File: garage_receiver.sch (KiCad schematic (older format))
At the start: 11 parts, among them J1 Conn_01x04_Female, J2 Screw_Terminal_01x04, Q1 2N7002, SW1 SW_DIP_x08, U1 HT12D

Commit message: DC/DC Converter
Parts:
- removed R1: 47k, Resistor_SMD:R_0805_2012Metric, symbol Device:R
- added C2: 47u, Capacitor_THT:CP_Radial_D5.0mm_P2.00mm, symbol Device:C
- added C3: 2.2u, Capacitor_THT:C_Disc_D4.3mm_W1.9mm_P5.00mm, symbol Device:C
- added D5: 1N5819, Diode_THT:D_DO-41_SOD81_P10.16mm_Horizontal, symbol Diode:1N5819
- added L1: 220u, Inductor_SMD:L_10.4x10.4_H4.8, symbol Device:L
- added Q2: 2N7002, Package_TO_SOT_SMD:SOT-23, symbol Transistor_FET:2N7002
- added R2: 1k, Resistor_SMD:R_0805_2012Metric, symbol Device:R
- added R3: 47k, Resistor_SMD:R_0805_2012Metric, symbol Device:R
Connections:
- net +12V: now also Q2.3 (D), R2.1; no longer D1.1 (K), D3.2 (A), J1.1 (Pin_1), U1.19 (VDD)
- net GND: now also D2.2 (A), D4.1 (K), C2.2, C3.2, D5.2 (A); no longer D3.1 (K), D4.2 (A), J2.2 (Pin_2), J2.3 (Pin_3), Q1.2 (S)
- net rf_data: now reaches J1.2 (Pin_2), J1.3 (Pin_3), U1.15 (DIN)
- net at U1.16 (OSC2): now also R3.2
- net at U1.17 (OSC1): now also R3.1
- net open: now reaches Q1.1 (G), U1.18 (VT)
- net door_control1: now reaches Q1.3 (D)
- net door_control1: now also J2.2 (Pin_2); no longer J2.1 (Pin_1)
- new net: D1.1 (K), D3.2 (A), R2.2
- new net: D5.1 (K), L1.1, Q2.2 (S)
- new net +5V: C2.1, C3.1, J1.1 (Pin_1), L1.2, U1.19 (VDD)
- new net GNDPWR: D3.1 (K), D4.2 (A), J2.3 (Pin_3)
- new net door_control2: J2.1 (Pin_1), Q1.2 (S)
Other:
- note added: "Actuator"
- note added: "DC/DC Converter"
- note added: "Decoder"
- note added: "RF 433/315MHz Receiver"
- note added: "Rectifier"
- note added: "Supply and Control Sinals"
- moved on the sheet: C1, D1, D2, D3, D4, J1, J2, Q1, SW1, U1

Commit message: DC/DC Converter Controller
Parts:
- removed D5: 1N5819, Diode_THT:D_DO-41_SOD81_P10.16mm_Horizontal, symbol Diode:1N5819
- removed Q2: 2N7002, Package_TO_SOT_SMD:SOT-23, symbol Transistor_FET:2N7002
- added C?: 1u, Capacitor_THT:CP_Radial_D4.0mm_P1.50mm, symbol Device:C
- added R1, R?: 100k, symbol Device:R
- added R?: 10k, symbol Device:R
- added R?: 2k, symbol Device:R
- added U2: MP1470, Package_TO_SOT_SMD:TSOT-23-6, symbol Regulator_Switching:MP1470
- L1: value 220u -> 33u
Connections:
- net +12V: now also R1.1, U2.3 (IN)
- net +5V: now also R?.1
- net GND: now also R?.1, U2.1 (GND)
- net at L1.1: now also C?.1, U2.2 (SW)
- new net: R?.2, U2.4 (FB)
- new net: R1.2, U2.5 (EN)
- new net: C?.2, U2.6 (BST)
- new net: R?.1, R?.2, R?.2
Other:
- note added: "Input Pins"
- note added: "RF Receiver"
- note removed: "RF 433/315MHz Receiver"
- note removed: "Supply and Control Sinals"
- moved on the sheet: C1, C2, C3, D1, D2, D3, D4, J1, J2, L1, Q1, R2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

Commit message: PCB Layout
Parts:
- R1: footprint (none) -> Resistor_SMD:R_0805_2012Metric
- R4, R5, R6: renamed from R?; footprint (none) -> Resistor_SMD:R_0805_2012Metric
- gave numbers to parts that had none: 1
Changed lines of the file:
@@
 F 0 "R1" H 5520 4346 50  0000 L CNN
 F 1 "100k" H 5520 4255 50  0000 L CNN
-F 2 "" V 5380 4300 50  0001 C CNN
+F 2 "Resistor_SMD:R_0805_2012Metric" V 5380 4300 50  0001 C CNN
 F 3 "~" H 5450 4300 50  0001 C CNN
 	1    5450 4300
@@
 	6850 4250 6850 4350
 $Comp
-L Device:C C?
+L Device:C C4
 U 1 1 5D5A52F5
 P 6700 4250
-F 0 "C?" V 6448 4250 50  0000 C CNN
+F 0 "C4" V 6448 4250 50  0000 C CNN
 F 1 "1u" V 6539 4250 50  0000 C CNN
 F 2 "Capacitor_THT:CP_Radial_D4.0mm_P1.50mm" H 6738 4100 50  0001 C CNN
@@
 $EndComp
 $Comp
-L Device:R R?
+L Device:R R4
 U 1 1 5D5D76B9
 P 6750 4650
-F 0 "R?" V 6543 4650 50  0000 C CNN
+F 0 "R4" V 6543 4650 50  0000 C CNN
 F 1 "100k" V 6634 4650 50  0000 C CNN
-F 2 "" V 6680 4650 50  0001 C CNN
+F 2 "Resistor_SMD:R_0805_2012Metric" V 6680 4650 50  0001 C CNN
 F 3 "~" H 6750 4650 50  0001 C CNN
 	1    6750 4650
@@
 	6550 4650 6600 4650
 $Comp
-L power:GND #PWR?
+L power:GND #PWR02
 U 1 1 5D5D9D52
 P 6100 4750
-F 0 "#PWR?" H 6100 4500 50  0001 C CNN
+F 0 "#PWR02" H 6100 4500 50  0001 C CNN
 F 1 "GND" H 6105 4577 50  0000 C CNN
 F 2 "" H 6100 4750 50  0001 C CNN
@@
 	6100 4750 6100 4650
 $Comp
-L Device:R R?
+L Device:R R5
 U 1 1 5D5DC077
 P 7150 4650
-F 0 "R?" V 6943 4650 50  0000 C CNN
+F 0 "R5" V 6943 4650 50  0000 C CNN
 F 1 "10k" V 7034 4650 50  0000 C CNN
-F 2 "" V 7080 4650 50  0001 C CNN
+F 2 "Resistor_SMD:R_0805_2012Metric" V 7080 4650 50  0001 C CNN
 F 3 "~" H 7150 4650 50  0001 C CNN
 	1    7150 4650
@@
 $EndComp
 $Comp
-L Device:R R?
+L Device:R R6
 U 1 1 5D5DC6C7
 P 6950 4900
-F 0 "R?" H 6880 4854 50  0000 R CNN
+F 0 "R6" H 6880 4854 50  0000 R CNN
 F 1 "2k" H 6880 4945 50  0000 R CNN
-F 2 "" V 6880 4900 50  0001 C CNN
+F 2 "Resistor_SMD:R_0805_2012Metric" V 6880 4900 50  0001 C CNN
 F 3 "~" H 6950 4900 50  0001 C CNN
 	1    6950 4900
@@
 Connection ~ 6950 4650
 $Comp
-L power:GND #PWR?
+L power:GND #PWR012
 U 1 1 5D5E3AF5
 P 6950 5100
-F 0 "#PWR?" H 6950 4850 50  0001 C CNN
+F 0 "#PWR012" H 6950 4850 50  0001 C CNN
 F 1 "GND" H 6955 4927 50  0000 C CNN
 F 2 "" H 6950 5100 50  0001 C CNN

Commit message: Prepare for production
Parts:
- added H1, H2, H3, H4: MountingHole, MountingHole:MountingHole_3.2mm_M3, symbol Mechanical:MountingHole
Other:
- note added: "Mounting Holes"
- moved on the sheet: C2, C3, C4, J1, L1, Q1, R1, R4, R5, R6, U2

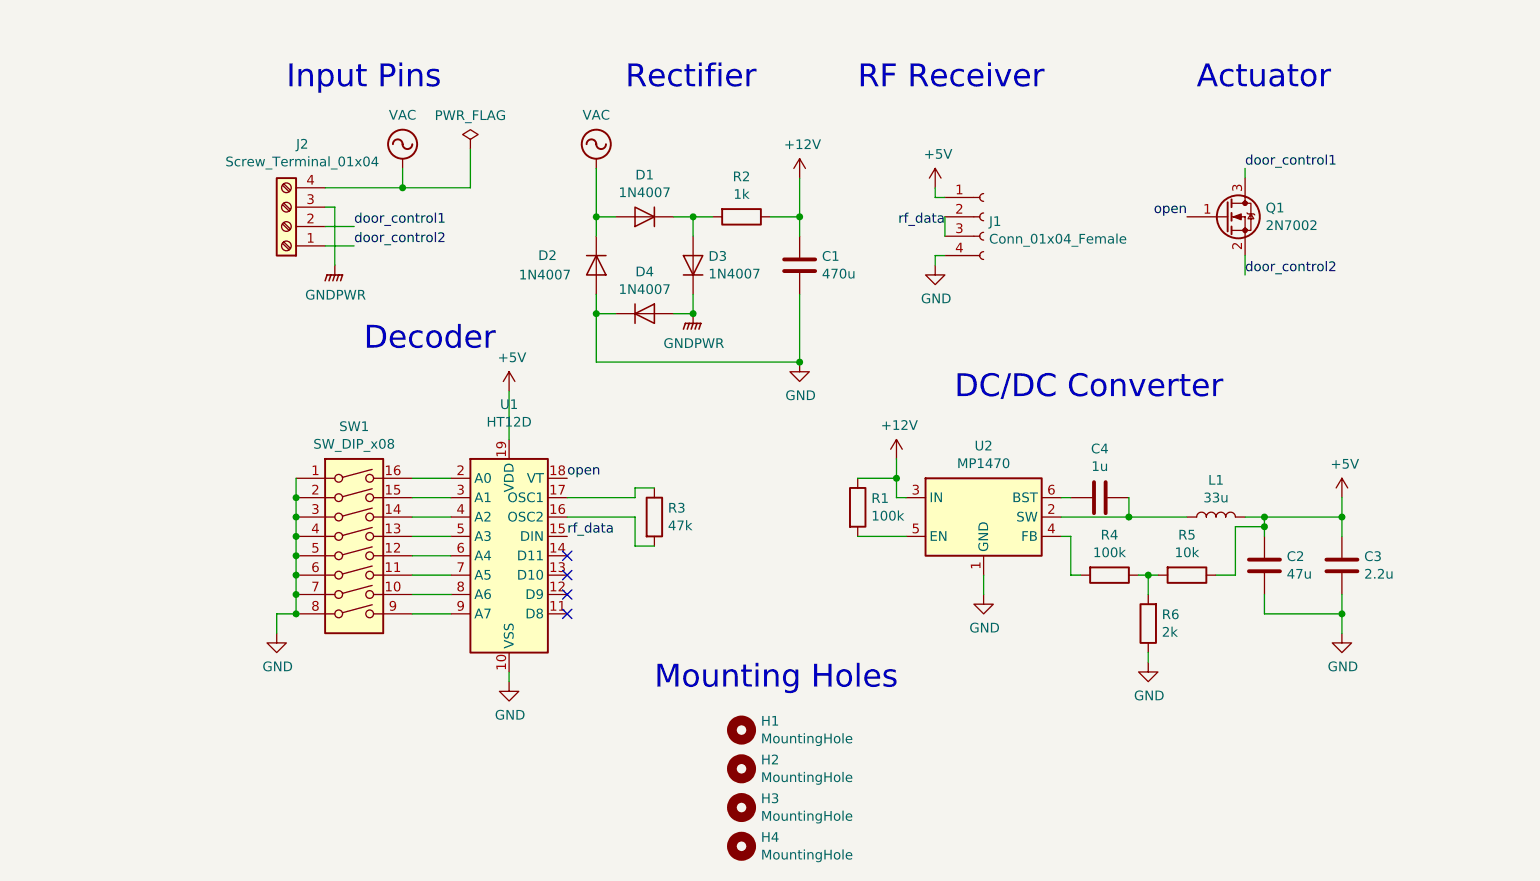
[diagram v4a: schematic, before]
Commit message: Change Control Pin Labels
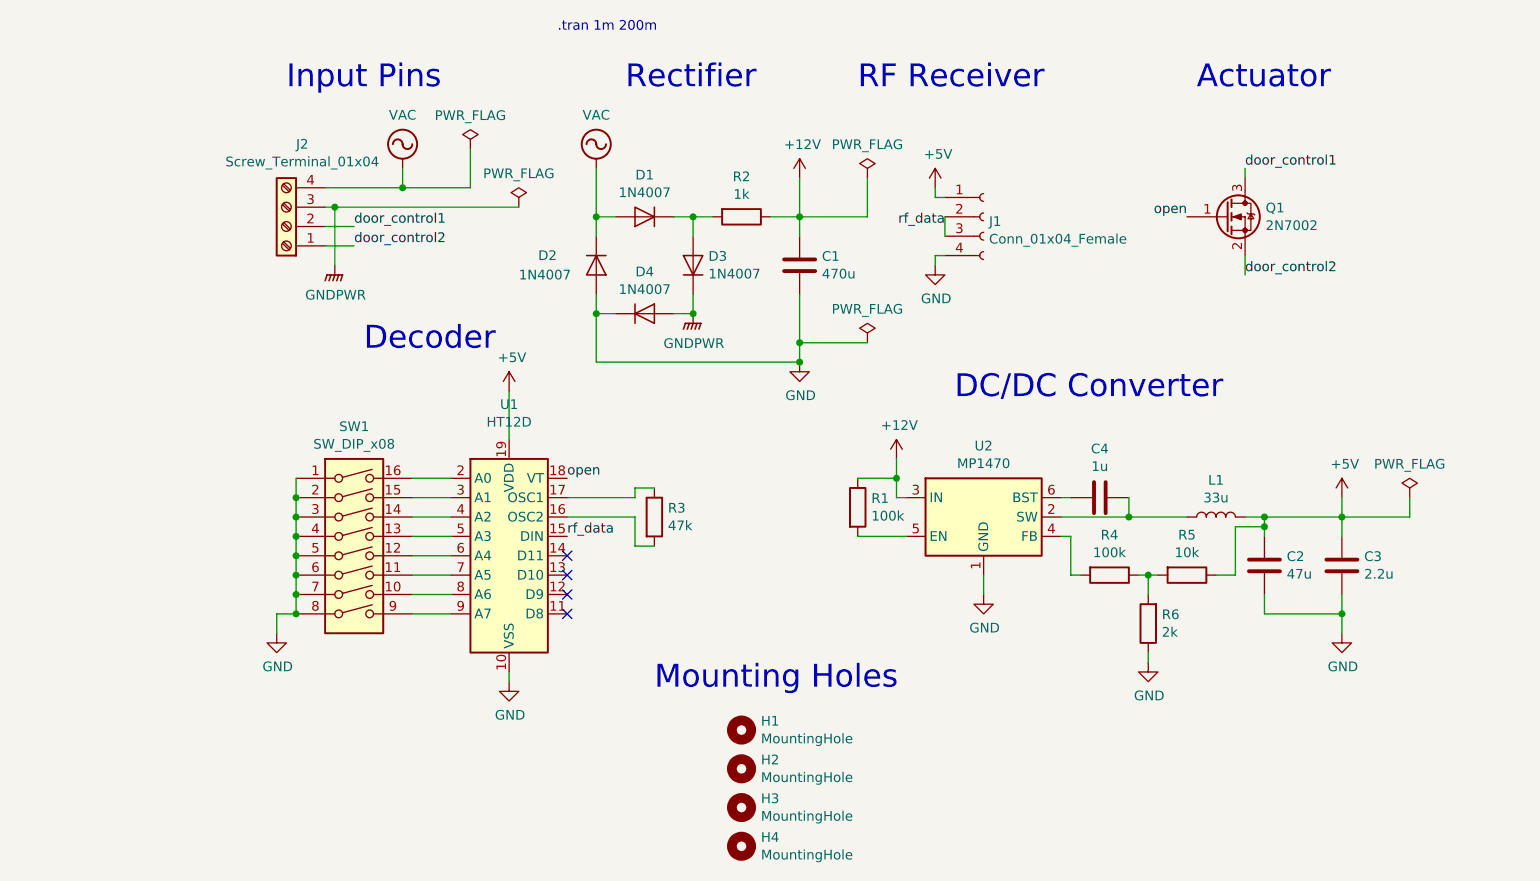
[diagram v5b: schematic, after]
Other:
- note added: ".tran 1m 200m"
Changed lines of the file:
@@
 Rectifier
 Wire Wire Line
-	5800 3100 5800 3450
+	5800 3100 5800 3350
 $Comp
 L power:GND #PWR08
@@
 Text Notes 5050 5150 0    118  ~ 0
 Mounting Holes
+Text Notes 4550 1750 0    50   ~ 0
+.tran 1m 200m
+$Comp
+L Mechanical:MountingHole H4
+U 1 1 5D79473A
+P 5500 5950
+F 0 "H4" H 5600 5996 50  0000 L CNN
+F 1 "MountingHole" H 5600 5905 50  0000 L CNN
+F 2 "MountingHole:MountingHole_3.2mm_M3" H 5500 5950 50  0001 C CNN
+F 3 "~" H 5500 5950 50  0001 C CNN
+	1    5500 5950
+	1    0    0    -1
+$EndComp
+$Comp
+L Mechanical:MountingHole H3
+U 1 1 5D794422
+P 5500 5750
+F 0 "H3" H 5600 5796 50  0000 L CNN
+F 1 "MountingHole" H 5600 5705 50  0000 L CNN
+F 2 "MountingHole:MountingHole_3.2mm_M3" H 5500 5750 50  0001 C CNN
+F 3 "~" H 5500 5750 50  0001 C CNN
+	1    5500 5750
+	1    0    0    -1
+$EndComp
+$Comp
+L Mechanical:MountingHole H2
+U 1 1 5D793FF2
+P 5500 5550
+F 0 "H2" H 5600 5596 50  0000 L CNN
+F 1 "MountingHole" H 5600 5505 50  0000 L CNN
+F 2 "MountingHole:MountingHole_3.2mm_M3" H 5500 5550 50  0001 C CNN
+F 3 "~" H 5500 5550 50  0001 C CNN
+	1    5500 5550
+	1    0    0    -1
+$EndComp
 $Comp
 L Mechanical:MountingHole H1
@@
 $EndComp
 $Comp
-L Mechanical:MountingHole H2
-U 1 1 5D793FF2
-P 5500 5550
-F 0 "H2" H 5600 5596 50  0000 L CNN
-F 1 "MountingHole" H 5600 5505 50  0000 L CNN
-F 2 "MountingHole:MountingHole_3.2mm_M3" H 5500 5550 50  0001 C CNN
-F 3 "~" H 5500 5550 50  0001 C CNN
-	1    5500 5550
-	1    0    0    -1
-$EndComp
-$Comp
-L Mechanical:MountingHole H3
-U 1 1 5D794422
-P 5500 5750
-F 0 "H3" H 5600 5796 50  0000 L CNN
-F 1 "MountingHole" H 5600 5705 50  0000 L CNN
-F 2 "MountingHole:MountingHole_3.2mm_M3" H 5500 5750 50  0001 C CNN
-F 3 "~" H 5500 5750 50  0001 C CNN
-	1    5500 5750
-	1    0    0    -1
-$EndComp
-$Comp
-L Mechanical:MountingHole H4
-U 1 1 5D79473A
-P 5500 5950
-F 0 "H4" H 5600 5996 50  0000 L CNN
-F 1 "MountingHole" H 5600 5905 50  0000 L CNN
-F 2 "MountingHole:MountingHole_3.2mm_M3" H 5500 5950 50  0001 C CNN
-F 3 "~" H 5500 5950 50  0001 C CNN
-	1    5500 5950
-	1    0    0    -1
-$EndComp
+L power:PWR_FLAG #FLG0102
+U 1 1 5D0FABAA
+P 6150 2500
+F 0 "#FLG0102" H 6150 2575 50  0001 C CNN
+F 1 "PWR_FLAG" H 6150 2673 50  0000 C CNN
+F 2 "" H 6150 2500 50  0001 C CNN
+F 3 "~" H 6150 2500 50  0001 C CNN
+	1    6150 2500
+	1    0    0    -1
+$EndComp
+Wire Wire Line
+	6150 2500 6150 2700
+Wire Wire Line
+	6150 2700 5800 2700
+$Comp
+L power:PWR_FLAG #FLG0103
+U 1 1 5D101C72
+P 8950 4150
+F 0 "#FLG0103" H 8950 4225 50  0001 C CNN
+F 1 "PWR_FLAG" H 8950 4323 50  0000 C CNN
+F 2 "" H 8950 4150 50  0001 C CNN
+F 3 "~" H 8950 4150 50  0001 C CNN
+	1    8950 4150
+	1    0    0    -1
+$EndComp
+Wire Wire Line
+	8950 4150 8950 4250
+Wire Wire Line
+	8950 4250 8600 4250
+$Comp
+L power:PWR_FLAG #FLG0104
+U 1 1 5D106776
+P 6150 3350
+F 0 "#FLG0104" H 6150 3425 50  0001 C CNN
+F 1 "PWR_FLAG" H 6150 3523 50  0000 C CNN
+F 2 "" H 6150 3350 50  0001 C CNN
+F 3 "~" H 6150 3350 50  0001 C CNN
+	1    6150 3350
+	1    0    0    -1
+$EndComp
+Wire Wire Line
+	6150 3350 5800 3350
+Connection ~ 5800 3350
+Wire Wire Line
+	5800 3350 5800 3450
+$Comp
+L power:PWR_FLAG #FLG0105
+U 1 1 5D10A97E
+P 4350 2650
+F 0 "#FLG0105" H 4350 2725 50  0001 C CNN
+F 1 "PWR_FLAG" H 4350 2823 50  0000 C CNN
+F 2 "" H 4350 2650 50  0001 C CNN
+F 3 "~" H 4350 2650 50  0001 C CNN
+	1    4350 2650
+	1    0    0    -1
+$EndComp
+Wire Wire Line
+	4350 2650 3400 2650
+Connection ~ 3400 2650
 $EndSCHEMATC

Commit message: Rotate Labels
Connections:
- net door_control2 is gone; now on net GND: J2.1 (Pin_1), Q1.2 (S)
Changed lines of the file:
@@
 	4350 2650 3400 2650
 Connection ~ 3400 2650
+$Comp
+L power:GND #PWR?
+U 1 1 5D0D959C
+P 8100 3000
+F 0 "#PWR?" H 8100 2750 50  0001 C CNN
+F 1 "GND" H 8105 2827 50  0000 C CNN
+F 2 "" H 8100 3000 50  0001 C CNN
+F 3 "" H 8100 3000 50  0001 C CNN
+	1    8100 3000
+	1    0    0    -1
+$EndComp
 $EndSCHEMATC

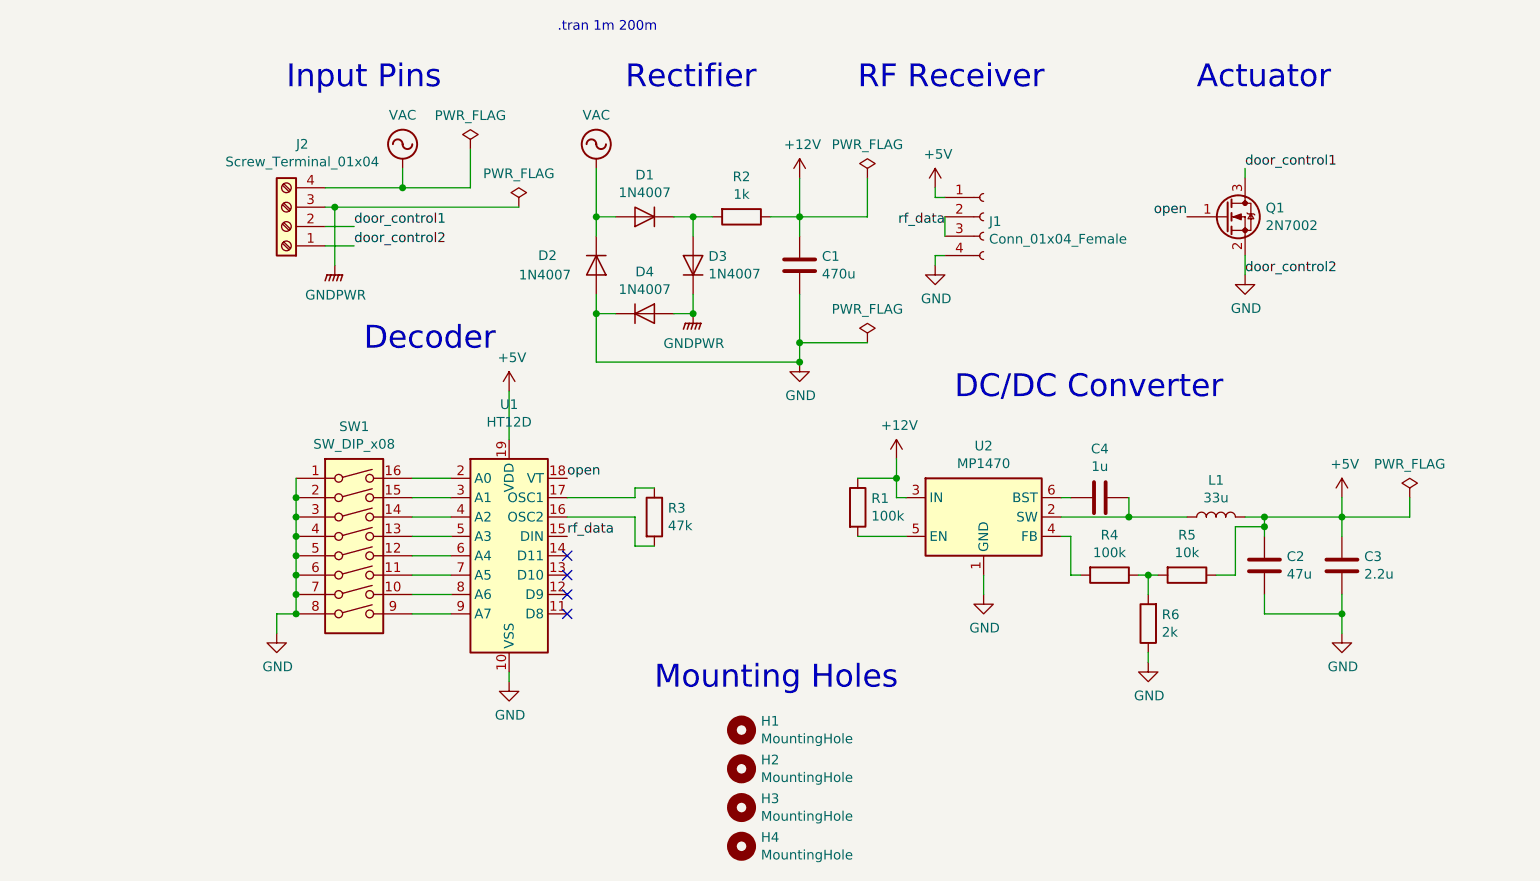
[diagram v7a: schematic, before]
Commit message: DC/DC converter updated to input range 4V to 48V
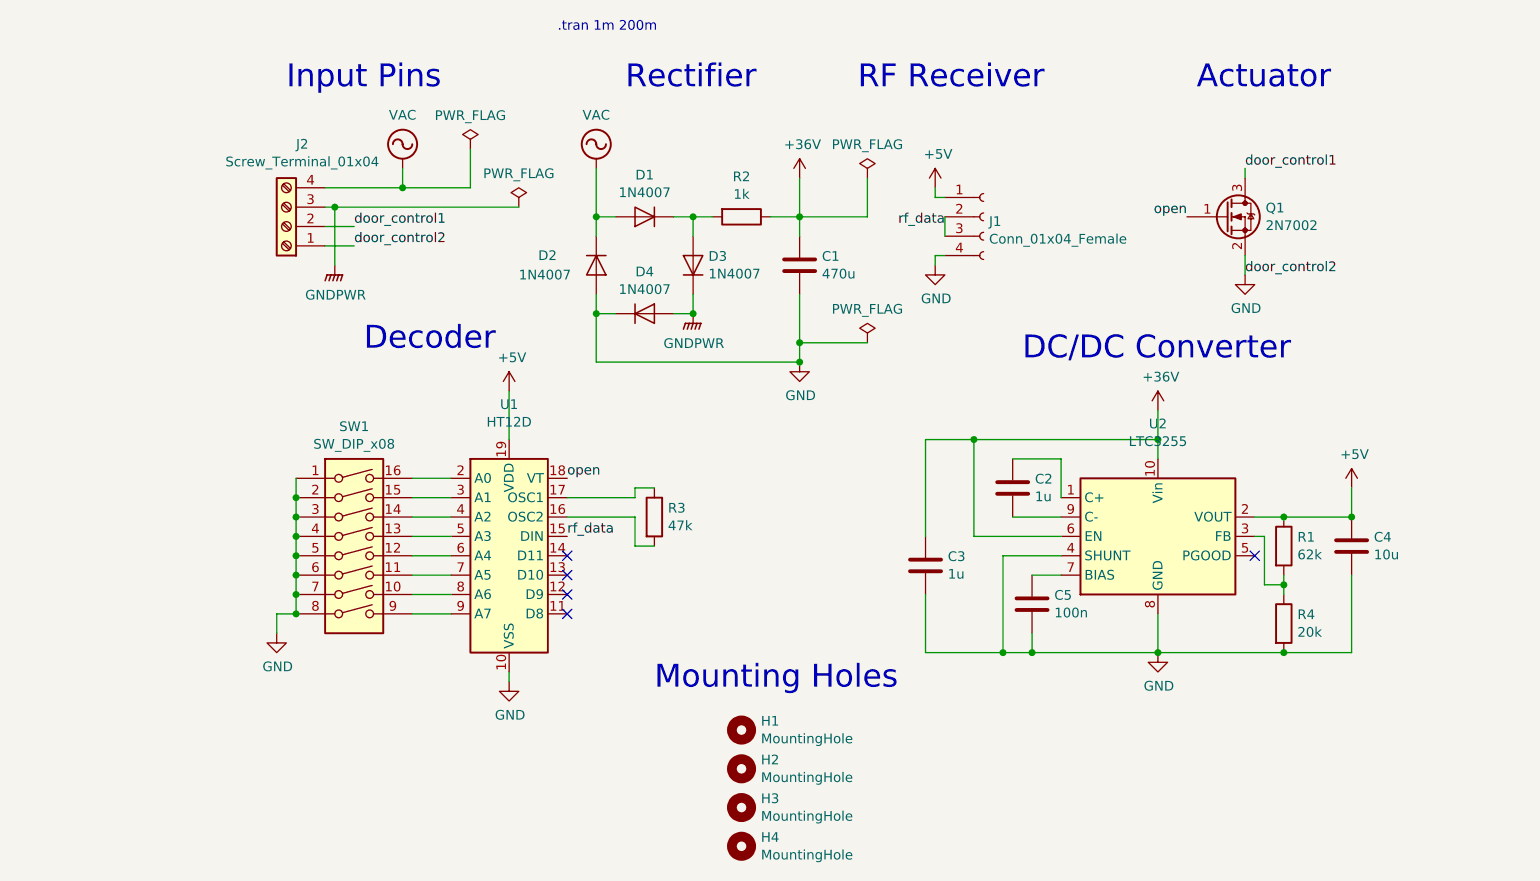
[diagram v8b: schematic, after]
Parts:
- removed L1: 33u, Inductor_SMD:L_10.4x10.4_H4.8, symbol Device:L
- removed R5: 10k, Resistor_SMD:R_0805_2012Metric, symbol Device:R
- removed R6: 2k, Resistor_SMD:R_0805_2012Metric, symbol Device:R
- removed U2: MP1470, Package_TO_SOT_SMD:TSOT-23-6, symbol Regulator_Switching:MP1470
- added C5: 100n, Capacitor_SMD:C_0805_2012Metric, symbol Device:C
- added U2: LTC3255, Package_SO:MSOP-10-1EP_3x3mm_P0.5mm_EP1.68x1.88mm_ThermalVias, symbol garage_receiver:LTC3255
- C2: value 47u -> 1u; footprint Capacitor_THT:CP_Radial_D5.0mm_P2.00mm -> Capacitor_SMD:C_0805_2012Metric
- C3: value 2.2u -> 1u; footprint Capacitor_THT:C_Disc_D4.3mm_W1.9mm_P5.00mm -> Capacitor_SMD:C_0805_2012Metric
- C4: value 1u -> 10u; footprint Capacitor_THT:CP_Radial_D4.0mm_P1.50mm -> Capacitor_SMD:C_0805_2012Metric
- H1, H2, H3, H4: footprint MountingHole:MountingHole_3.2mm_M3 -> MountingHole:MountingHole_3.2mm_M3_Pad_Via
- R1: value 100k -> 62k
- R4: value 100k -> 20k
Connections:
- net +5V: now also C4.1, R1.1, U2.2 (VOUT); no longer C2.1, C3.1
- net GND: now also C4.2, R4.2, C5.2, U2.11 (GND), U2.4 (SHUNT), U2.8 (GND); no longer C2.2
- net at R1.2: now also R4.1, U2.3 (FB)
- net +12V renamed +36V
- net +36V: now also C3.1, U2.10 (Vin), U2.6 (EN); no longer R1.1
- new net: C2.1, U2.1 (C+)
- new net: C2.2, U2.9 (C-)
- new net: C5.1, U2.7 (BIAS)
- no-connect marks 4 -> 5
